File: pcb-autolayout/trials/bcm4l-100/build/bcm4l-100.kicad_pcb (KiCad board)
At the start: 4 copper layers, 80 x 60 mm, 120 parts, among them J1 MicroFit 2x4, J2 MicroFit 2x6, J3 SWD, Q1 SQD40P06 (P-MOS), Q11 AO3401A, Q12 MMBT3904, Q13 AO3401A, Q14 MMBT3904, Q15 AO3401A, Q16 MMBT3904, Q17 AO3401A, Q18 MMBT3904, SW1 RESET, U1 TPS54202, U2 AMS1117-3.3, U3 TJA1051T/3, U4 TJA1021T/20, U5 STM32F103C8T6, Y1 8MHz

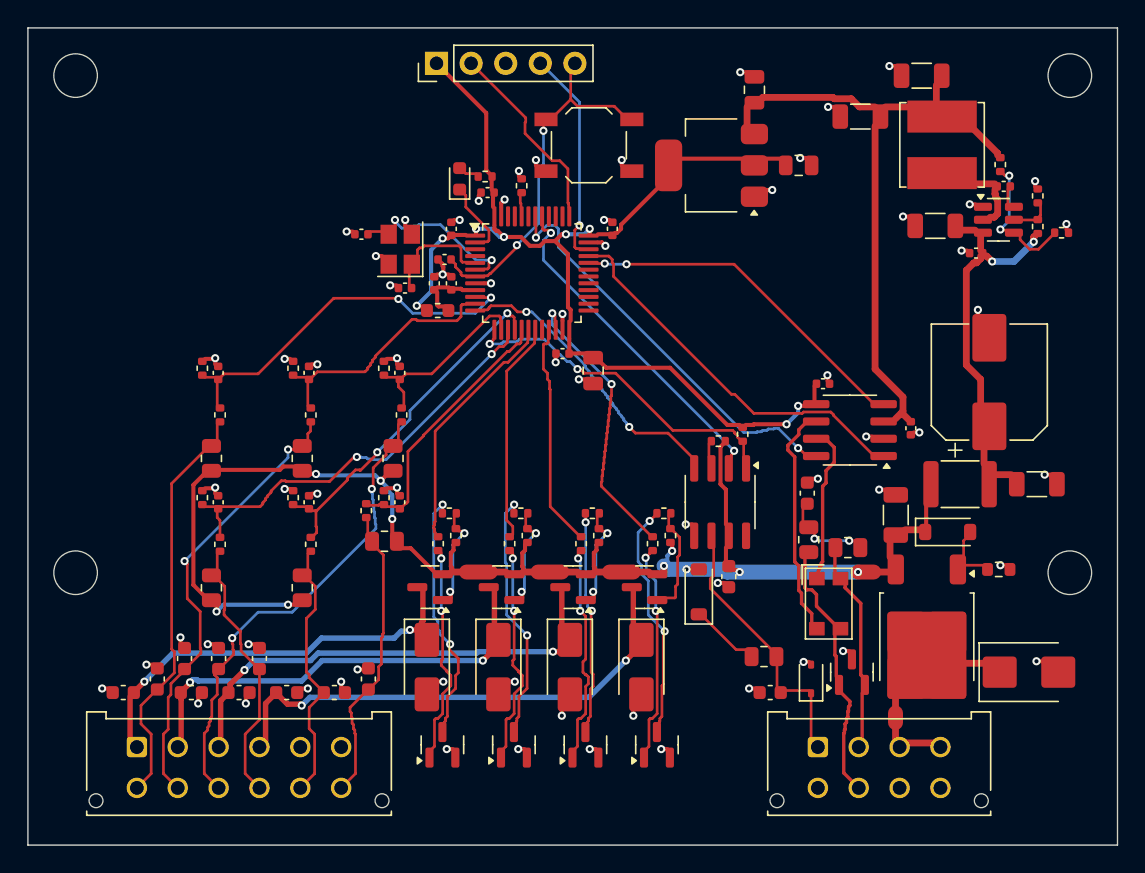
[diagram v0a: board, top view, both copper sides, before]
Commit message: pcb-autolayout: polish pass, GND pour+stitching, silk placer, rules_lint, SKILL.md
- T24 polish: re-route each net with hard obstacles, no history, higher
  bend cost; keep only if complete and shorter (1069 -> 802 segments)
- T22 stitching: GND pours on outer layers, grid + edge-ring stitching
  vias; EMC-021 rule and checker
- Deterministic silkscreen reference placer (DRC warnings 0)
- T36 rules_lint + per-rule checker tests
- Skill packaging: .claude/skills/pcb-autolayout/SKILL.md
- CONFORMANCE.md: plan vs current state, including deviations

Trial: KiCad DRC 0 errors/0 warnings/0 unconnected, 11/11 rules,
byte-identical output across two runs.

Co-Authored-By: Claude Opus 5.5 <noreply@anthropic.com>
Claude-Session: https://claude.ai/code/session_012jwodCpQFB8wopi3P3TnUz
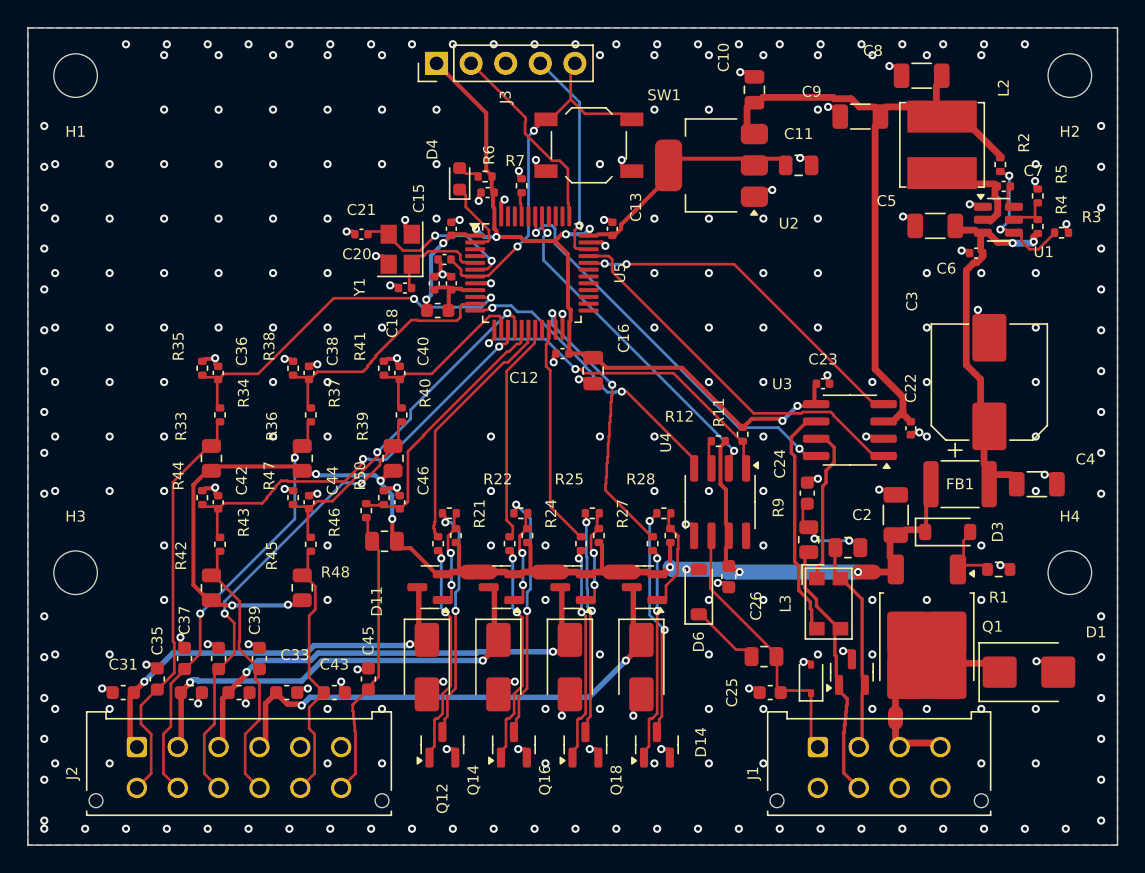
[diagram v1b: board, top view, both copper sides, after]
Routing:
- net VBAT_P: track 84.8 -> 83.0 mm, vias 10 -> 9
- net +3V3: track 67.7 -> 66.0 mm
- net OUT1_C: track 18.0 -> 16.4 mm
- net IN2: track 30.7 -> 29.3 mm
- net OSC_IN: track 6.13 -> 5.16 mm
- net CAN_S: track 29.0 -> 28.1 mm
- net VBAT_F: track 21.9 -> 21.1 mm
- net OUT4_C: track 16.7 -> 16.0 mm
- net LIN_TX: track 20.8 -> 20.2 mm
- net OUT1_G: track 6.44 -> 5.90 mm
- net OUT3_G: track 6.44 -> 5.90 mm
- net OUT2_G: track 6.44 -> 5.90 mm
- net OSC_OUT: track 10.9 -> 10.4 mm
- net GND: vias 67 -> 288
- added copper zone on B.Cu, net GND
- added copper zone on F.Cu, net GND

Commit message: pcb-autolayout: fixes from independent hardware and engine reviews
Circuit: 60 V buck (EN from LIN INH), bidirectional TVS, 60 V P-FETs
with Vgs zener clamp, NPN base pull-downs, power-rated resistors,
corrected CMC winding map, ceramic-stable LDO, safer ADC divider.

Engine: probe A* source cells; group rip-up so routing ends with zero
overlap (RT-CLR); per-netclass clearance in router and exported to
KiCad via .kicad_dru; neck-down only near small pads; no vias on >=1 A
nets plus via reinforcement; via-to-pad gap; THT hole clearance;
integer-nm coordinates; full UUID remap in canonicalize; T16 layout
templates with self-check; placer clock priority, ratline-through-pad
penalty, region growth, per-part allowed rotations.

Rules: PWR-001 rewritten, new RT-CLR, PWR-005, DFM-005, SMPS-004,
SI-070; 16 rules with tests. Trial: 16/16 rules, KiCad DRC clean,
deterministic hash 10125c887e9c1a41.

Co-Authored-By: Claude Opus 5.5 <noreply@anthropic.com>
Claude-Session: https://claude.ai/code/session_012jwodCpQFB8wopi3P3TnUz
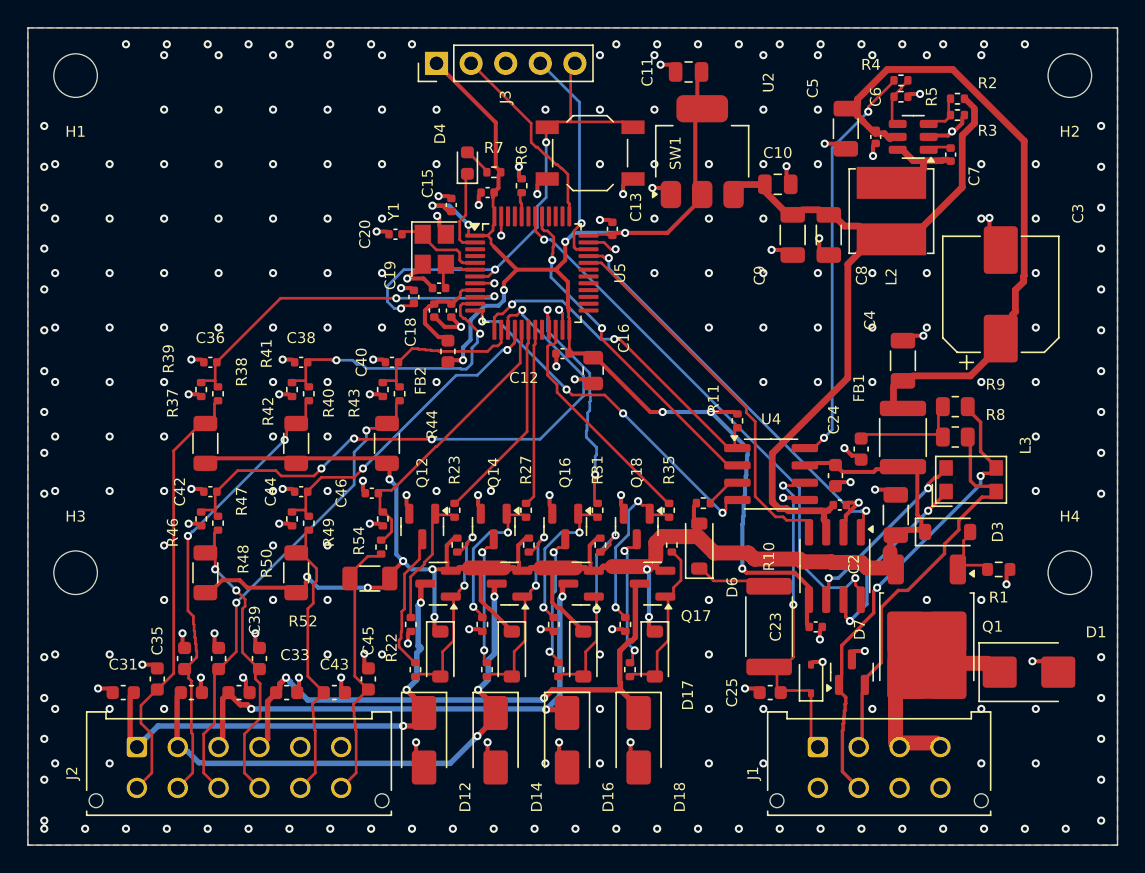
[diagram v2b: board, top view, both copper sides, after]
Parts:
- removed the R34 at (114.1, 88.4)
- removed the R35 at (112.8, 85.0)
- removed the R38 at (119.5, 85.0)
- removed the R44 at (112.8, 94.5)
- removed the R47 at (119.5, 94.5)
- added D17: BZT52C10, Diode_SMD:D_SOD-123, F.Cu at (146.0, 106.0)
- added D3: BZT52C10, Diode_SMD:D_SOD-123, F.Cu at (167.5, 97.0)
- added D6: 1N4148W, Diode_SMD:D_SOD-123, F.Cu at (149.3, 98.0)
- added D7: PESD1LIN, Diode_SMD:D_SOD-323, F.Cu at (157.5, 107.8)
- added R1: 10k, Resistor_SMD:R_0603_1608Metric, F.Cu at (171.3, 99.8)
- added R10: 1k 1W, Resistor_SMD:R_2512_6332Metric, F.Cu at (154.4, 104.0)
- added R37: 4k7, Resistor_SMD:R_1206_3216Metric, F.Cu at (113.0, 90.5)
- added R40: 4k7, Resistor_SMD:R_1206_3216Metric, F.Cu at (119.7, 90.5)
- added R46: 4k7, Resistor_SMD:R_1206_3216Metric, F.Cu at (113.0, 100.0)
- added R49: 4k7, Resistor_SMD:R_1206_3216Metric, F.Cu at (119.7, 100.0)
- added R52: 4k7, Resistor_SMD:R_1206_3216Metric, F.Cu at (125.1, 100.4)
- added R8: 60R4, Resistor_SMD:R_0805_2012Metric, F.Cu at (168.1, 90.0)
- added R9: 60R4, Resistor_SMD:R_0805_2012Metric, F.Cu at (168.1, 87.8)
- C10: renamed from C11; value 22u -> 10u
- C11: renamed from C10; value 10u -> 22u
- C19: renamed from C20; value 20p -> 100n
- C2: renamed from C5; value 10u 50V -> 100n 100V
- C20: renamed from C46; value 10n -> 15p
- C21: renamed from C19; value 100n -> 15p
- C25: renamed from C26; value 100n 50V -> 1n 50V
- C26: renamed from C25; value 1n 50V -> 100n 50V
- C3: value 47u 35V -> 47u 63V
- C4: value 4u7 50V -> 2u2 100V
- C46: renamed from C21; value 20p -> 10n
- C5: renamed from C8; value 22u 10V -> 4u7 100V
- C6: value 100n 50V -> 100n 100V
- C8: renamed from C2; value 100n 50V -> 22u 10V
- D1: value SMBJ24A -> SMBJ33CA
- D11: renamed from D6; value BAS21 -> BZT52C10
- D15: renamed from D7; value ESD LIN -> BZT52C10; footprint Diode_SMD:D_SOD-323 -> Diode_SMD:D_SOD-123
- L2: value 10u -> 22u
- Q11, Q13, Q15, Q17: value AO3401A -> ZXMP6A13F -60V
- R11: renamed from R48; value 2k2 -> 4k7; footprint Resistor_SMD:R_0805_2012Metric -> Resistor_SMD:R_0402_1005Metric
- R12: renamed from R36; value 2k2 -> 10k; footprint Resistor_SMD:R_0805_2012Metric -> Resistor_SMD:R_0402_1005Metric
- R2: renamed from R9; value 60R4 -> 100k; footprint Resistor_SMD:R_0805_2012Metric -> Resistor_SMD:R_0402_1005Metric
- R25: renamed from R11; value 4k7 -> 10k
- R26: renamed from R32; value 1k -> 10k
- R27: renamed from R12; value 10k -> 1k
- R29: renamed from R3; value 13k7 -> 10k
- R3: renamed from R8; value 60R4 -> 18k; footprint Resistor_SMD:R_0805_2012Metric -> Resistor_SMD:R_0402_1005Metric
- R30: renamed from R5; value 22k -> 10k
- R31: renamed from R4; value 100k -> 1k
- R32: renamed from R2; value 100k -> 10k
- R33: renamed from R45; value 2k2 -> 10k; footprint Resistor_SMD:R_0805_2012Metric -> Resistor_SMD:R_0402_1005Metric
- R34: renamed from R42; value 2k2 -> 10k; footprint Resistor_SMD:R_0805_2012Metric -> Resistor_SMD:R_0402_1005Metric
- R35: renamed from R33; value 2k2 -> 1k; footprint Resistor_SMD:R_0805_2012Metric -> Resistor_SMD:R_0402_1005Metric
- R36: renamed from R1; footprint Resistor_SMD:R_0603_1608Metric -> Resistor_SMD:R_0402_1005Metric
- R38: renamed from R49; value 47k -> 82k
- R39: renamed from R37; value 47k -> 10k
- R4: renamed from R39; value 2k2 -> 10k; footprint Resistor_SMD:R_0805_2012Metric -> Resistor_SMD:R_0402_1005Metric
- R41: renamed from R23; value 1k -> 82k
- R43: value 47k -> 4k7; footprint Resistor_SMD:R_0402_1005Metric -> Resistor_SMD:R_1206_3216Metric
- R44: renamed from R25; value 10k -> 82k
- R45: renamed from R7; value 1k -> 10k
- R47: renamed from R41; value 10k -> 82k
- R48: renamed from R46; value 47k -> 10k
- R5: renamed from R10; value 1k -> 100k; footprint Resistor_SMD:R_0805_2012Metric -> Resistor_SMD:R_0402_1005Metric
- R50: renamed from R22; value 10k -> 82k
- R51: renamed from R40; value 47k -> 10k
- R53: renamed from R21; value 10k -> 82k
- R54: renamed from R26; value 1k -> 10k
- R7: renamed from R31; value 10k -> 1k
- U1: value TPS54202 -> LMR16006X-Q1
- U2: value AMS1117-3.3 -> TLV1117LV33-Q1
- moved R30 49.5 mm to (139.0, 107.1)
- moved R32 47.1 mm to (138.6, 103.8)
- moved R4 46.5 mm to (164.1, 63.9), turned to 0 degrees
- moved R5 42.3 mm to (164.1, 65.0)
- moved R29 40.9 mm to (142.0, 98.0), turned to -90 degrees
- moved R31 38.5 mm to (141.8, 95.4), turned to -90 degrees
- moved R2 34.2 mm to (168.2, 65.2), turned to 180 degrees
- moved R35 33.8 mm to (147.1, 95.4), turned to -90 degrees
- moved D13 33.2 mm to (135.5, 106.0), turned to -90 degrees
- moved R24 33.2 mm to (128.1, 103.8), turned to -90 degrees
- moved R3 32.8 mm to (168.2, 66.4)
- moved R34 31.3 mm to (144.2, 107.1)
- moved R12 29.6 mm to (149.6, 94.9), turned to 180 degrees
- moved R7 28.0 mm to (134.2, 70.6)
- moved R6 27.9 mm to (136.2, 71.6)
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- renumbered D11 to D12, D3 to D13, D12 to D14, D13 to D16, D14 to D18, R28 to R21, R24 to R22, R29 to R23, R6 to R24, R27 to R28, R50 to R42, R30 to R6
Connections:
- C10 pad 1: +3V3 -> +5V
- C11 pad 1: +5V -> +3V3
- C19 pad 1: OSC_IN -> NRST
- C2 pad 1: VBAT_F -> VBAT_P
- C20 pad 1: IN6_M -> OSC_IN
- C21 pad 1: NRST -> OSC_OUT
- C25 pad 1: VBAT_P -> LIN
- C26 pad 1: LIN -> VBAT_P
- C46 pad 1: OSC_OUT -> IN6_M
- C5 pad 1: +5V -> VBAT_F
- C8 pad 1: VBAT_P -> +5V
- D11 pad 1: LIN_PU -> VBAT_P
- D11 pad 2: VBAT_P -> OUT1_G
- D13 pad 2: Q1_G -> OUT2_G
- D15 pad 1: LIN -> VBAT_P
- D15 pad 2: GND -> OUT3_G
- L3 pad 2: CANL_T -> CANH
- L3 pad 4: CANH -> CANL_T
- R11 pad 1: VBAT_P -> LIN_RX
- R11 pad 2: IN6 -> +3V3
- R12 pad 1: VBAT_P -> LIN_WAKE
- R12 pad 2: IN2 -> VBAT_P
- R2 pad 1: CANL -> +5V
- R2 pad 2: CAN_SPL -> FB5
- R21 pad 1: OUT3_G -> VBAT_P
- R21 pad 2: OUT3_C -> OUT1_G
- R22 pad 1: VBAT_P -> OUT1_G
- R22 pad 2: OUT2_G -> OUT1_C
- R23 pad 1: OUT3_M -> OUT1_M
- R23 pad 2: OUT3_B -> OUT1_B
- R24 pad 1: BOOT0 -> OUT1_B
- R25 pad 1: LIN_RX -> VBAT_P
- R25 pad 2: +3V3 -> OUT2_G
- R26 pad 1: OUT4_M -> OUT2_G
- R26 pad 2: OUT4_B -> OUT2_C
- R27 pad 1: LIN_WAKE -> OUT2_M
- R27 pad 2: VBAT_P -> OUT2_B
- R28 pad 1: VBAT_P -> OUT2_B
- R28 pad 2: OUT3_G -> GND
- R29 pad 1: FB5 -> VBAT_P
- R29 pad 2: GND -> OUT3_G
- R3 pad 1: CANH -> FB5
- R3 pad 2: CAN_SPL -> GND
- R30 pad 1: EN5 -> OUT3_G
- R30 pad 2: GND -> OUT3_C
- R31 pad 1: VBAT_F -> OUT3_M
- R31 pad 2: EN5 -> OUT3_B
- R32 pad 1: +5V -> OUT3_B
- R32 pad 2: FB5 -> GND
- R33 pad 2: IN5 -> OUT4_G
- R34 pad 1: VBAT_P -> OUT4_G
- R34 pad 2: IN4 -> OUT4_C
- R35 pad 1: VBAT_P -> OUT4_M
- R35 pad 2: IN1 -> OUT4_B
- R36 pad 1: Q1_G -> OUT4_B
- R38 pad 1: IN6 -> IN1
- R38 pad 2: IN6_M -> IN1_M
- R39 pad 1: IN2 -> IN1_M
- R39 pad 2: IN2_M -> GND
- R4 pad 1: VBAT_P -> LIN_INH
- R4 pad 2: IN3 -> EN5
- R41 pad 1: OUT1_M -> IN2
- R41 pad 2: OUT1_B -> IN2_M
- R42 pad 1: IN6_M -> IN2_M
- R43 pad 1: IN4 -> VBAT_P
- R43 pad 2: IN4_M -> IN3
- R44 pad 1: OUT2_G -> IN3
- R44 pad 2: OUT2_C -> IN3_M
- R45 pad 1: +3V3 -> IN3_M
- R45 pad 2: LED_A -> GND
- R47 pad 1: IN3_M -> IN4
- R47 pad 2: GND -> IN4_M
- R48 pad 1: IN5 -> IN4_M
- R48 pad 2: IN5_M -> GND
- R5 pad 1: LIN_PU -> EN5
- R5 pad 2: LIN -> GND
- R50 pad 1: OUT1_G -> IN5
- R50 pad 2: OUT1_C -> IN5_M
- R51 pad 1: IN3 -> IN5_M
- R51 pad 2: IN3_M -> GND
- R53 pad 1: VBAT_P -> IN6
- R53 pad 2: OUT1_G -> IN6_M
- R54 pad 1: OUT2_M -> IN6_M
- R54 pad 2: OUT2_B -> GND
- R6 pad 1: VBAT_P -> BOOT0
- R6 pad 2: OUT4_G -> GND
- R7 pad 1: OUT4_G -> +3V3
- R7 pad 2: OUT4_C -> LED_A
- U1 pad 1: GND -> BOOT5
- U1 pad 2: SW5 -> GND
- U1 pad 3: VBAT_F -> FB5
- U1 pad 4: FB5 -> EN5
- U1 pad 5: EN5 -> VBAT_F
- U1 pad 6: BOOT5 -> SW5
- U4 pad 8: (no net) -> LIN_INH
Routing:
- net GND: track 36.4 -> 65.5 mm, vias 288 -> 282
- net LIN_INH: track 0.00 -> 28.9 mm, vias 0 -> 2
- net +3V3: track 66.0 -> 90.7 mm, vias 8 -> 9
- net VBAT_P: track 83.0 -> 106.3 mm, vias 9 -> 8
- net VBAT_F: track 21.1 -> 40.8 mm, vias 2 -> 0
- net CANL: track 16.4 -> 31.2 mm, vias 0 -> 2
- net CANH: track 12.4 -> 25.8 mm
- net IN4_M: track 29.2 -> 41.9 mm, vias 2 -> 4
- net CAN_S: track 28.1 -> 39.0 mm
- net NRST: track 22.5 -> 33.0 mm, vias 2 -> 3
- net OUT3_G: track 5.90 -> 14.5 mm
- net OUT2_C: track 17.4 -> 8.81 mm
- net OSC_OUT: track 10.4 -> 1.99 mm, vias 2 -> 0
- net OUT1_G: track 5.90 -> 12.9 mm
- net OUT2_G: track 5.90 -> 12.9 mm
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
